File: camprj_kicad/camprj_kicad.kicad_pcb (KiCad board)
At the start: 2 copper layers, 85 x 56 mm, 120 parts, among them J1 ESQ-120-69-G-D-LL, J2 USB_OTG, U1 LM3670SOT23-5, U10 MAX1561, U11 MAX1561, U12 MAX1561, U13 MAX1561, U14 MAX1561, U15 MAX1561, U16 BQ24075RGTR, U2 Molex 1052028-1001, U3 ADP150AUJZ-3.3-R7, U4 ADP150AUJZ-2.8-R7, U5 ADP150AUJZ-3.3-R7, U6 VL53L0X, U7 ADP150AUJZ-3.3-R7, U8 FIS1100, U9 ADP150AUJZ-1.8-R7, Y1 ASFLMB-25MHZ

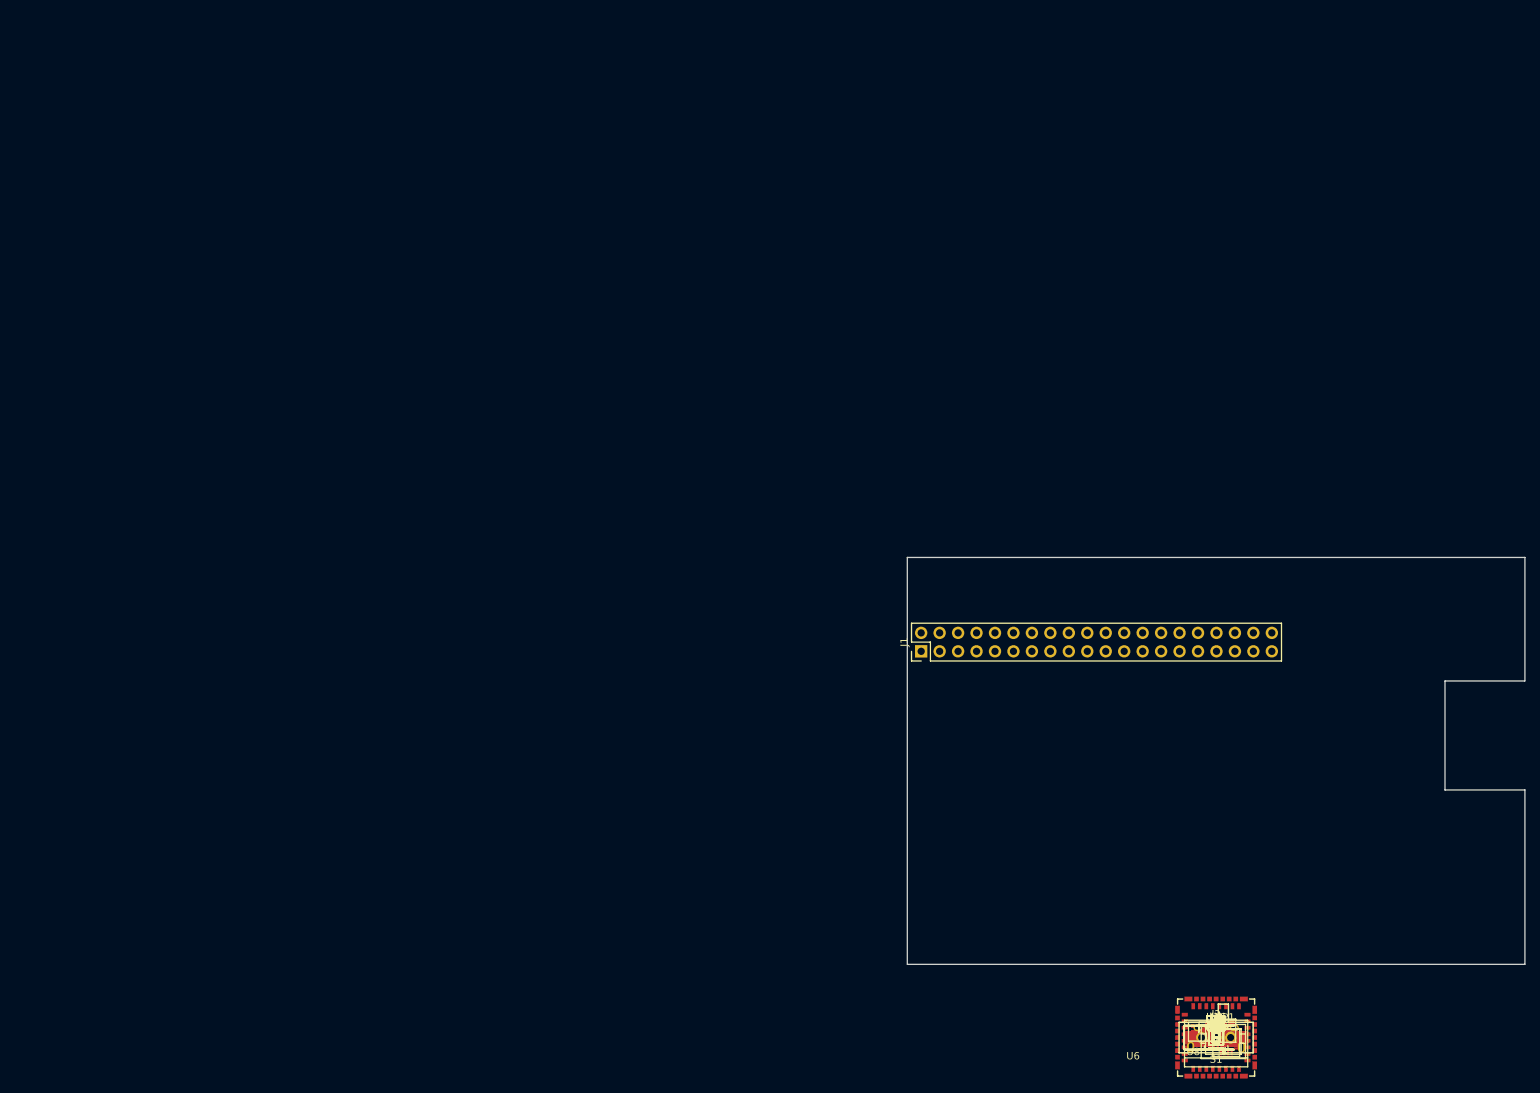
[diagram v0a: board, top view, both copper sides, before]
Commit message: Board design: component placement done
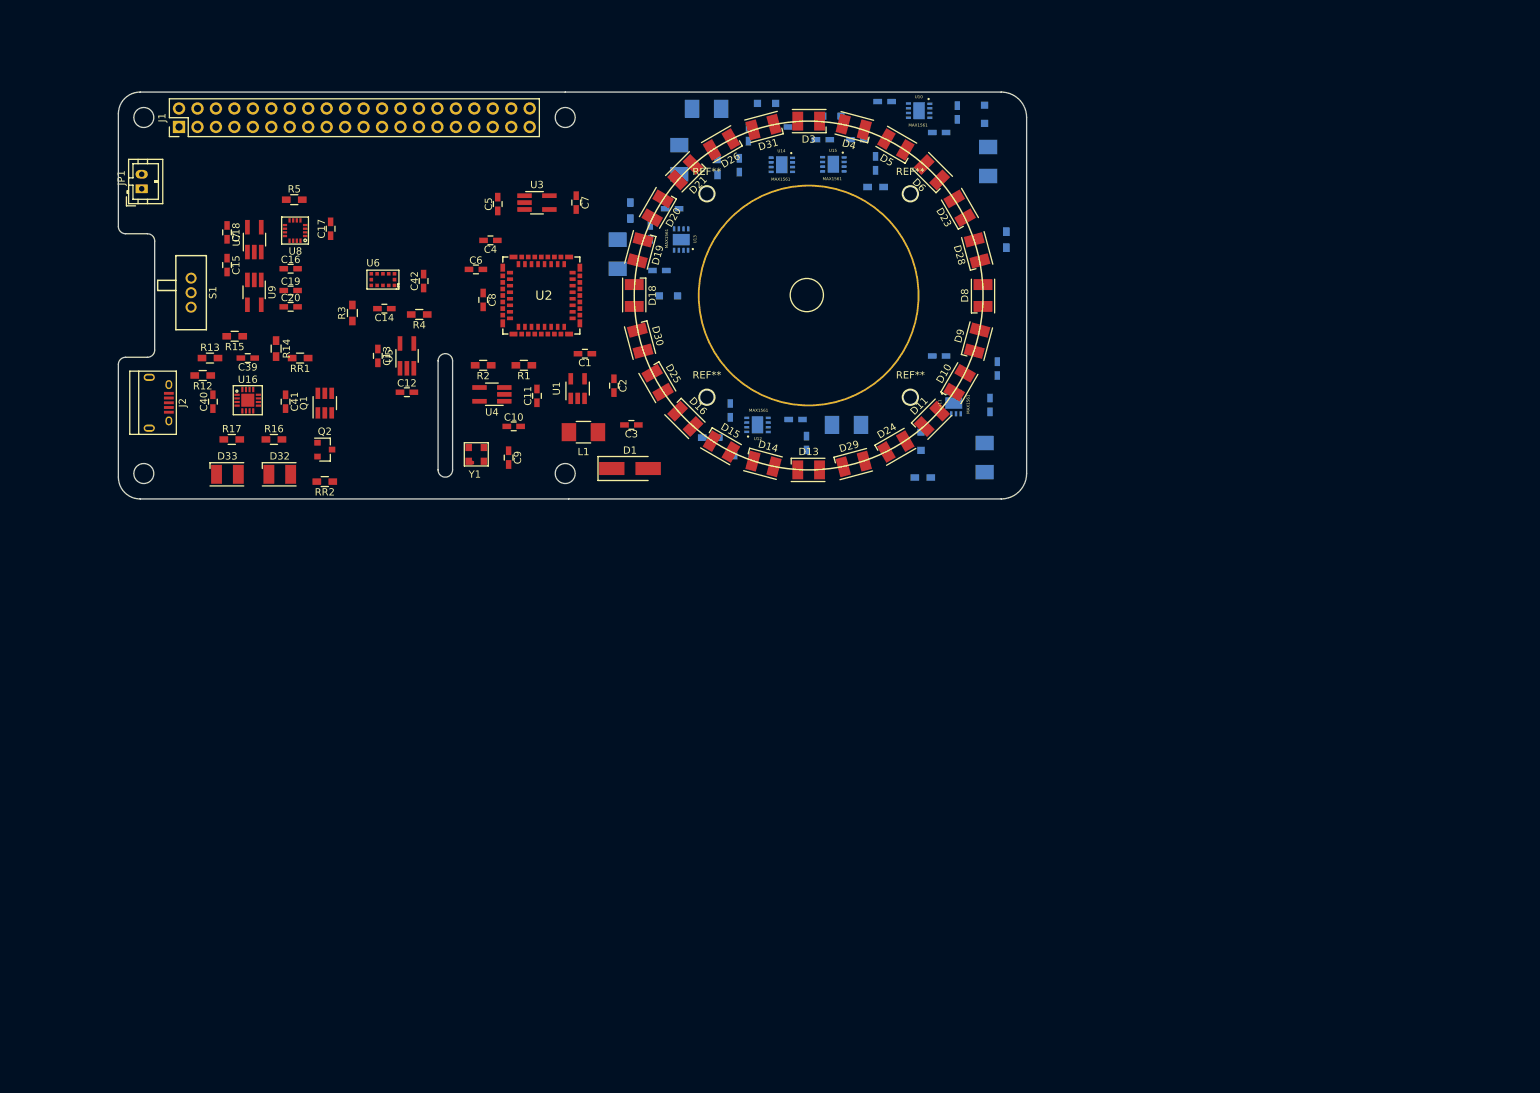
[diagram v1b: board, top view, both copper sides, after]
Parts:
- added ?: , RPi_Hat:RPi_Hat_Mounting_Hole, F.Cu at (159.3, 63.7)
- added ?: , RPi_Hat:RPi_Hat_Mounting_Hole, F.Cu at (159.3, 112.7)
- added ?: , RPi_Hat:RPi_Hat_Mounting_Hole, F.Cu at (101.3, 112.7)
- added ?: , RPi_Hat:RPi_Hat_Mounting_Hole, F.Cu at (101.3, 63.7)
- added Q1: DMMT5401, TO_SOT_Packages_SMD:SOT-23-6_Handsoldering, F.Cu at (126.2, 103.0)
- added Q2: DMG2305UX, TO_SOT_Packages_SMD:SOT-23, F.Cu at (126.2, 109.4)
- added REF**: 1pin, Connectors:1pin, F.Cu at (192.5, 88.1)
- added REF**: 1pin, Myfootprints:1pin_2mm, F.Cu at (178.8, 74.2)
- added REF**: 1pin, Myfootprints:1pin_2mm, F.Cu at (206.8, 74.2)
- added REF**: 1pin, Myfootprints:1pin_2mm, F.Cu at (206.8, 102.2)
- added REF**: 1pin, Myfootprints:1pin_2mm, F.Cu at (178.8, 102.2)
- added RR1: 10K, Resistors_SMD:R_0603_HandSoldering, F.Cu at (122.8, 96.8)
- added RR2: 47K, Resistors_SMD:R_0603_HandSoldering, F.Cu at (126.2, 113.8)
- C21, C22, C23, C24, C25, C26, C27, C28, C29, C30, C31, C32, C33, C34, C35, C36, C37, C38, L2, L3, L4, L5, L6, L7, R10, R11, R6, R7, R8, R9, U10, U11, U12, U13, U14, U15: moved to B.Cu
- D12, D17, D2, D22, D27, D7: value B340A -> CMDSH2-3; footprint Myfootprints:D_SMA_Handsoldering_AC -> Diodes_SMD:D_SOD-323_HandSoldering; moved to B.Cu
- J1: value ESQ-120-69-G-D-LL -> 20x2 header
- JP1: value SPARKFUN-CONNECTORS_JST_2MM_MALE -> JST_2MM_MALE
- moved JP1 188.4 mm to (101.0, 73.5), turned to 90 degrees
- moved C18 175.5 mm to (112.8, 79.5), turned to 270 degrees
- moved S1 174.4 mm to (107.8, 87.8), turned to 90 degrees
- moved C15 172.7 mm to (112.8, 84.0), turned to 270 degrees
- moved U7 172.0 mm to (116.5, 80.5), turned to 90 degrees
- moved R5 171.4 mm to (122.0, 75.0)
- moved J2 169.7 mm to (103.4, 103.0), turned to 270 degrees
- moved U9 167.5 mm to (116.5, 87.8), turned to 270 degrees
- moved R13 167.1 mm to (110.4, 96.8)
- moved U8 167.0 mm to (123.5, 80.0), turned to 180 degrees
- moved R12 166.6 mm to (109.4, 99.2), turned to 180 degrees
- moved R15 166.0 mm to (113.8, 93.8), turned to 180 degrees
- moved C16 165.6 mm to (121.5, 84.5)
- moved C17 165.1 mm to (127.0, 79.0), turned to 90 degrees
- moved C19 163.7 mm to (121.5, 87.5)
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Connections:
- net /LED_Drive/sheet5960845C/PWM_IN renamed /LED_Drive/IR_SET3/PWM_IN
- C41 pad 1: V5_0 -> Net-(C41-Pad1)
- D1 pad A: /thermal_sense/VIN -> V5_0
- D1 pad C: V5_0 -> /thermal_sense/VIN
- L2 pad 2: Net-(D2-PadA) -> Net-(D2-Pad1)
- L3 pad 2: Net-(D7-PadA) -> Net-(D7-Pad1)
- L4 pad 2: Net-(D12-PadA) -> Net-(D12-Pad1)
- L5 pad 2: Net-(D17-PadA) -> Net-(D17-Pad1)
- L6 pad 2: Net-(D22-PadA) -> Net-(D22-Pad1)
- L7 pad 2: Net-(D27-PadA) -> Net-(D27-Pad1)
- R16 pad 1: V5_0 -> Net-(C41-Pad1)
- R17 pad 1: V5_0 -> Net-(C41-Pad1)
- U10 pad 8: Net-(D2-PadA) -> Net-(D2-Pad1)
- U10 pad 9: (no net) -> GND
- U11 pad 8: Net-(D7-PadA) -> Net-(D7-Pad1)
- U11 pad 9: (no net) -> GND
- U12 pad 8: Net-(D12-PadA) -> Net-(D12-Pad1)
- U12 pad 9: (no net) -> GND
- U13 pad 8: Net-(D17-PadA) -> Net-(D17-Pad1)
- U13 pad 9: (no net) -> GND
- U14 pad 8: Net-(D22-PadA) -> Net-(D22-Pad1)
- U14 pad 9: (no net) -> GND
- U15 pad 8: Net-(D27-PadA) -> Net-(D27-Pad1)
- U15 pad 9: (no net) -> GND
- U16 pad 10: V5_0 -> Net-(C41-Pad1)
- U16 pad 11: V5_0 -> Net-(C41-Pad1)
- U16 pad 5: V5_0 -> Net-(C41-Pad1)
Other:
- board size 85 x 56 mm -> 125 x 56 mm
- net class Default: trace_width 0.2 -> 0.35; via_dia 0.9 -> 0.6; via_drill 0.6 -> 0.4
- net class Power removed
- rule trace_min: 0.1524 -> 0.15
- rule via_min_drill: 0.5 -> 0.3
- rule via_min_size: 0.8 -> 0.4
- board text added: "120mm"
- board text added: "Camera Flex Slot (Optional)"
- board text added: "Dimensions taken from https://github.com/raspberrypi/hats/blob/master/hat-board-mechanical.pdf"
- board text removed: "1/8" JACK OK WITH STD HEADERS !NO TH ABOVE!"
- board text removed: "DOUBLE USB CUTOUT FOR ALL BOARDS"
- board text removed: "RASPBERRY-PI ADDON BOARD VIEW FROM TOP NOTE: P1 SHOULD BE FITTED ON THE REVERSE OF THE BOARD"
- board text removed: "RCA REMOVE WITH STD HEADERS !NO TH ABOVE!"
- board text removed: "RJ45 CUTOUT FOR STD HEADERS !NO TH ABOVE!"

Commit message: routing done
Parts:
- U2: footprint 105028-1001:105028-1001 -> Myfootprints:105028-1001
- moved L6 6.83 mm to (168.2, 68.5)
- moved R10 6.67 mm to (174.6, 67.0)
- moved L7 4.55 mm to (174.2, 62.3)
- moved C33 4.16 mm to (180.8, 64.0)
- moved U14 2.57 mm to (186.6, 69.7)
- moved C17 2.40 mm to (129.4, 79.3)
- moved C34 2.28 mm to (181.0, 70.3)
- moved C37 1.53 mm to (203.5, 70.0)
- moved C25 1.50 mm to (211.1, 95.0), turned to 180 degrees
- moved R5 1.44 mm to (123.2, 75.7)
- moved U8 1.21 mm to (124.7, 79.9)
- moved C21 0.76 mm to (213.6, 63.7)
- moved U10 0.41 mm to (207.9, 63.1)
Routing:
- net GND: track 0.00 -> 510.2 mm, vias 0 -> 22
- net V5_0: track 0.00 -> 383.2 mm, vias 0 -> 24
- net LED_GPI_IR: track 0.00 -> 166.2 mm, vias 0 -> 8
- net LED_GPI_UV: track 0.00 -> 86.3 mm, vias 0 -> 4
- net VDDIO_TH: track 0.00 -> 79.9 mm, vias 0 -> 4
- net /thermal_sense/VIN: track 0.00 -> 79.6 mm, vias 0 -> 8
- net SDA: track 0.00 -> 76.2 mm, vias 0 -> 5
- net LED_GPI_WH: track 0.00 -> 75.3 mm, vias 0 -> 2
- net SCL: track 0.00 -> 72.2 mm, vias 0 -> 4
- net Net-(D30-Pad1): track 0.00 -> 57.0 mm, vias 0 -> 2
- net DIST_GPIO2: track 0.00 -> 54.5 mm, vias 0 -> 4
- net DIST_GPIO1: track 0.00 -> 44.7 mm, vias 0 -> 1
- net IMU_GPO1: track 0.00 -> 42.9 mm, vias 0 -> 3
- net +BATT: track 0.00 -> 42.8 mm, vias 0 -> 3
- net Net-(C38-Pad1): track 0.00 -> 42.8 mm, vias 0 -> 1
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- added copper zone on F.Cu, net GND
- added copper zone on B.Cu, net V5_0

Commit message: Final Delivery
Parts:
- added G***: LOGO, logo:mhsl_exported, F.Cu at (138.4, 75.0)
- added G***: LOGO, logo:eth_logo_exported, F.Cu at (135.6, 108.5)
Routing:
- net V5_0: track 383.2 -> 356.5 mm, vias 24 -> 23
- net Net-(D25-Pad1): track 41.8 -> 34.4 mm
- net GND: track 510.2 -> 506.6 mm
- net Net-(U8-Pad4): track 1.74 -> 0.14 mm
- net Net-(U8-Pad5): track 1.24 -> 0.14 mm
- net Net-(L1-Pad2): track 13.6 -> 12.6 mm
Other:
- outline, holes or cut-outs redrawn
- net class Default: clearance 0.2 -> 0.199; trace_width 0.35 -> 0.3; via_dia 0.6 -> 0.7
- net class Supply added: clearance 0.199, trace_width 0.6, via_dia 0.9, via_drill 0.4
- rule trace_clearance: 0.2 -> 0.199
- rule trace_min: 0.15 -> 0.16
- rule via_min_size: 0.4 -> 0.3
- board text added: "VitalCam v2.0 Geethan K. 02.08.2017"
- board text removed: "Dimensions taken from https://github.com/raspberrypi/hats/blob/master/hat-board-mechanical.pdf"
